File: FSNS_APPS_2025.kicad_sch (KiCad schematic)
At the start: 85 parts, among them J1 Conn_01x04_Pin, J2 Conn_01x03_Pin, J3 Conn_01x03_Pin, J4 Conn_01x02_Socket, K1 PR12-12V-360-1A, Q1 NDT3055L, SW1 SW_Push, U1 STM32F103C8T6, U2 MCP6001-OT, U3 MCP6001-OT, U4 LM1117-Q1, U5 LM1117-Q1, U6 LM1117-Q1, U7 TCAN3404-Q1, U8 LM1117-Q1, Y1 16MHz

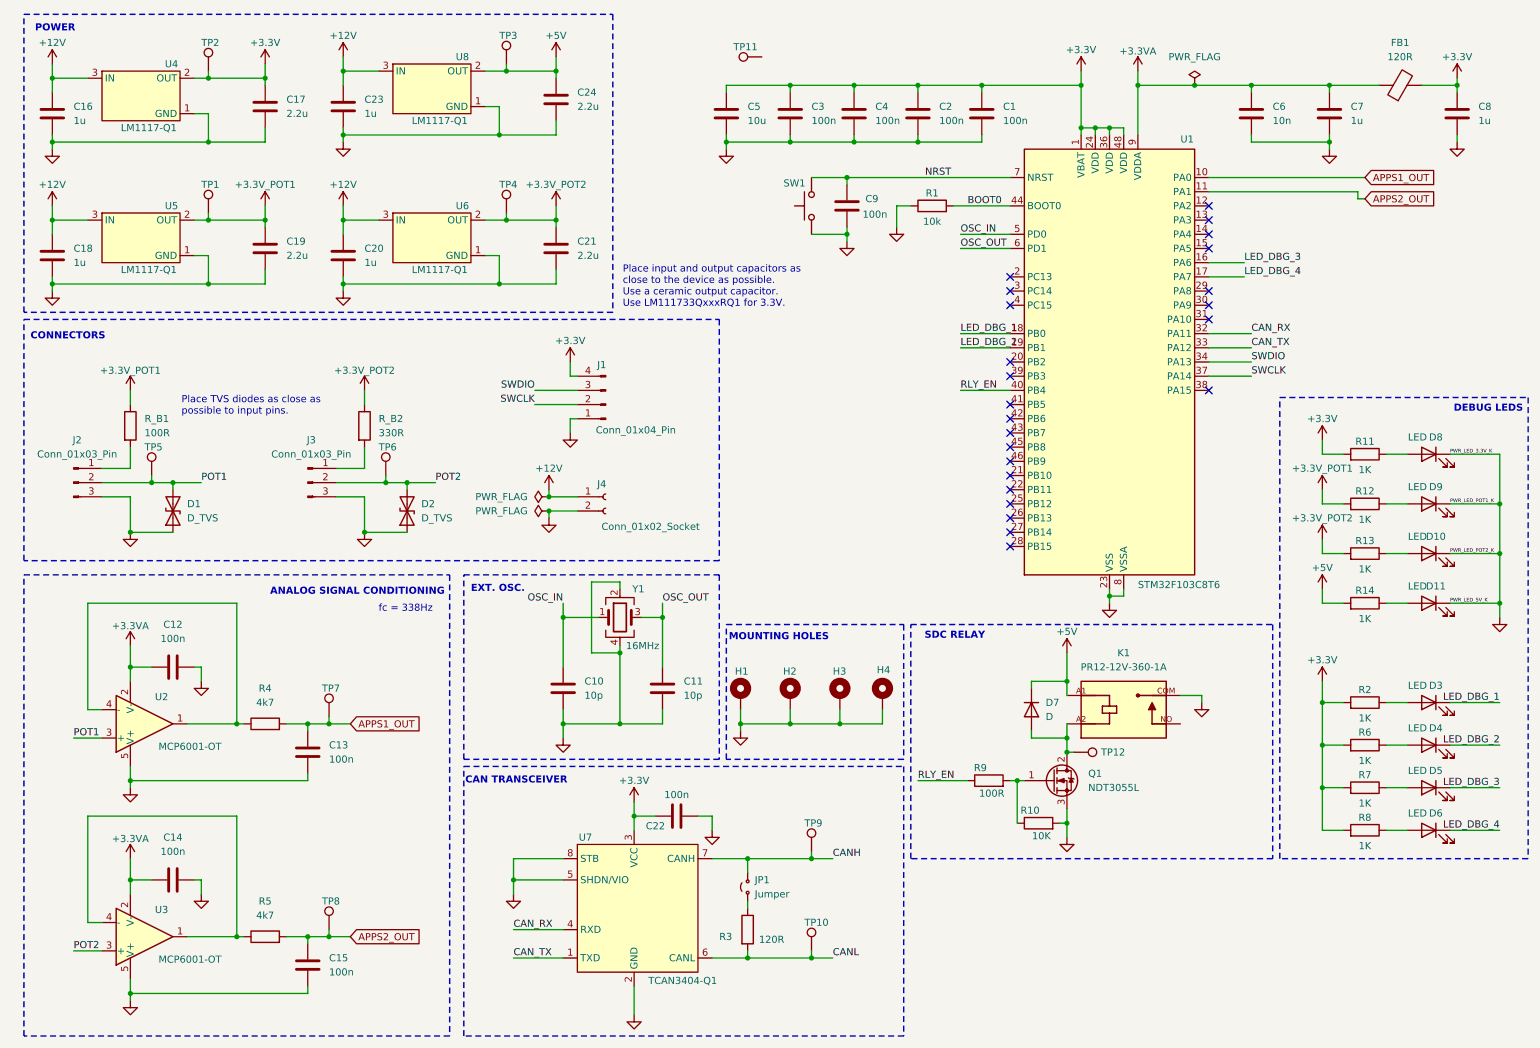
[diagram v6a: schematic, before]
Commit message: Updated schematic and PCB.
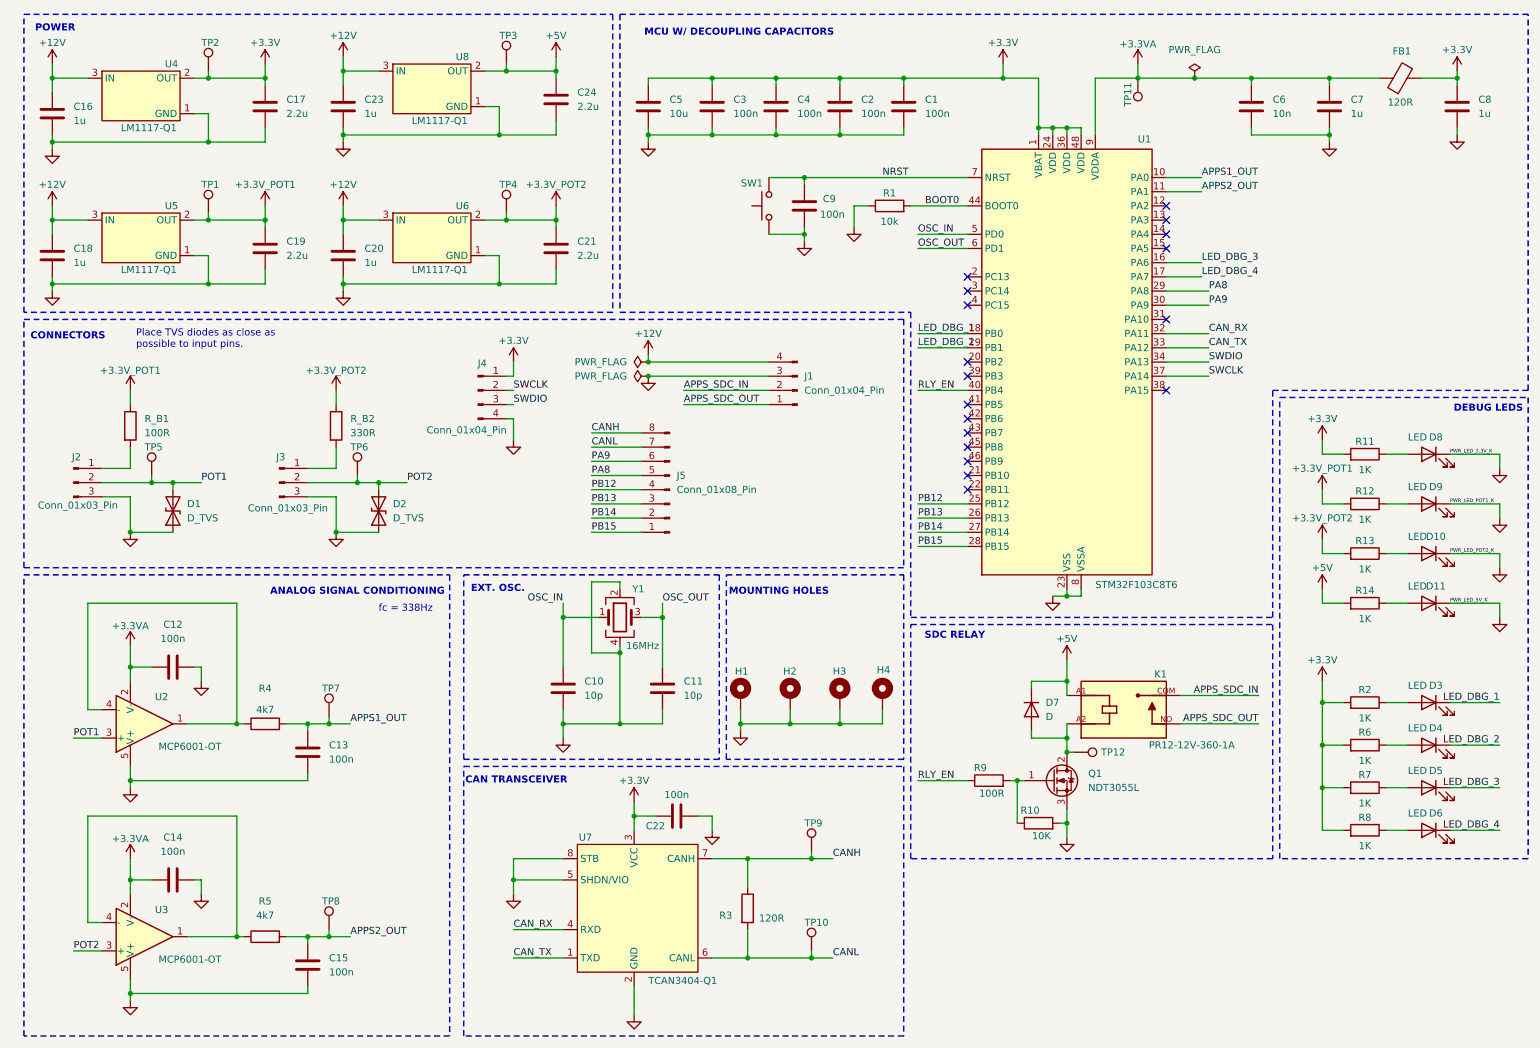
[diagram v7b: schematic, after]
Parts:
- removed J4: Conn_01x02_Socket, symbol Connector:Conn_01x02_Socket
- removed JP1: Jumper, symbol Jumper:Jumper_2_Small_Open
- added J4: Conn_01x04_Pin, Connector_PinHeader_2.54mm:PinHeader_1x04_P2.54mm_Horizontal, symbol Connector:Conn_01x04_Pin
- added J5: Conn_01x08_Pin, Connector_PinSocket_2.54mm:PinSocket_1x08_P2.54mm_Horizontal, symbol Connector:Conn_01x08_Pin
- D1, D2: footprint (none) -> Diode_SMD:D_0603_1608Metric
- D7: footprint (none) -> Diode_SMD:D_1206_3216Metric
- J1: footprint (none) -> MOLEX Micro-Fit 3.0 43045:CONN_SD-43045-005_04_MOL
- J2, J3: footprint (none) -> MOLEX Micro-Fit 3.0 43045:CONN_SD-43650-006_03_MOL
- R3: footprint (none) -> Resistor_SMD:R_0402_1005Metric
- SW1: footprint (none) -> Button_Switch_SMD:SW_SPST_B3S-1000
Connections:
- net +12V: now also J1.4 (Pin_4)
- net +3.3V: now also J4.1 (Pin_1); no longer J1.4 (Pin_4)
- net +3.3VA: now also TP11.1
- net CANH: now also R3.1, J5.8 (Pin_8)
- net CANL: now also J5.7 (Pin_7)
- net GND: now also J1.3 (Pin_3), J4.4 (Pin_4); no longer J1.1 (Pin_1), K1.COM
- net SWCLK: now also J4.2 (Pin_2); no longer J1.2 (Pin_2)
- net SWDIO: now also J4.3 (Pin_3); no longer J1.3 (Pin_3)
- net APPS_SDC_OUT: now reaches K1.NO
- net APPS_SDC_OUT: now also J1.1 (Pin_1)
- net PB12: now reaches U1.25 (PB12)
- net PB12: now also J5.4 (Pin_4)
- net PB13: now reaches U1.26 (PB13)
- net PB13: now also J5.3 (Pin_3)
- net PB14: now reaches U1.27 (PB14)
- net PB14: now also J5.2 (Pin_2)
- net PB15: now reaches U1.28 (PB15)
- net PB15: now also J5.1 (Pin_1)
- net PA8: now reaches U1.29 (PA8)
- net PA8: now also J5.5 (Pin_5)
- net PA9: now reaches U1.30 (PA9)
- net PA9: now also J5.6 (Pin_6)
- new net APPS_SDC_IN: J1.2 (Pin_2), K1.COM
- no-connect marks 24 -> 18
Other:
- note added: "MCU W/ DECOUPLING CAPACITORS"
- note removed: "Place input and output capacitors as close to the device as possible. Use a ceramic output capacitor. Use LM111733QxxxRQ1 for 3.3V."
- moved on the sheet: C1, C2, C3, C4, C5, C6, C7, C8, C9, D2, FB1, J3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

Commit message: Schematic and PCB v0.1
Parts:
- added JP1: SolderJumper_2_Open, symbol Jumper:SolderJumper_2_Open
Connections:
- net CANH: now also JP1.2 (B); no longer R3.1
- net PB12: now also J5.1 (Pin_1); no longer J5.4 (Pin_4)
- net PB13: now also J5.2 (Pin_2); no longer J5.3 (Pin_3)
- net PB14: now also J5.3 (Pin_3); no longer J5.2 (Pin_2)
- net PB15: now also J5.4 (Pin_4); no longer J5.1 (Pin_1)
- new net: JP1.1 (A), R3.1
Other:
- company: (none) -> Black Hornets Novi Sad - Predrag Nuzdic
- title: (none) -> Accelerator Pedal Position Sensor Board
- moved on the sheet: J5, R3
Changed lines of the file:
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@@
 	(generator_version "9.0")
 	(paper "A4")
+	(title_block
+		(title "Accelerator Pedal Position Sensor Board")
+		(date "2026-01-11")
+		(rev "0.1")
+		(company "Black Hornets Novi Sad - Predrag Nuzdic")
+	)
 	(rectangle
 		(start 92.71 113.03)
@@
 	)
 	(junction
+		(at 143.51 163.83)
+		(diameter 0)
+		(color 0 0 0 0)
+	)
+	(junction
 		(at 33.02 187.96)
 		(diameter 0)
@@
 	)
 	(junction
-		(at 143.51 163.83)
-		(diameter 0)
-		(color 0 0 0 0)
-	)
-	(junction
 		(at 46.99 35.56)
 		(diameter 0)
@@
 	(wire
 		(pts
-			(xy 115.57 87.63) (xy 124.46 87.63)
+			(xy 138.43 87.63) (xy 147.32 87.63)
 		)
 		(stroke
@@
 	(wire
 		(pts
+			(xy 143.51 163.83) (xy 143.51 165.1)
+		)
+		(stroke
+			(width 0)
+			(type default)
+		)
+	)
+	(wire
+		(pts
 			(xy 160.02 33.02) (xy 160.02 34.29)
 		)
@@
 	(wire
 		(pts
-			(xy 115.57 90.17) (xy 124.46 90.17)
+			(xy 138.43 90.17) (xy 147.32 90.17)
 		)
 		(stroke
@@
 	(wire
 		(pts
-			(xy 115.57 97.79) (xy 124.46 97.79)
+			(xy 138.43 105.41) (xy 147.32 105.41)
 		)
 		(stroke
@@
 	(wire
 		(pts
-			(xy 143.51 163.83) (xy 154.94 163.83)
+			(xy 137.16 163.83) (xy 143.51 163.83)
 		)
 		(stroke
@@
 	(wire
 		(pts
-			(xy 115.57 100.33) (xy 124.46 100.33)
+			(xy 138.43 102.87) (xy 147.32 102.87)
 		)
 		(stroke
@@
 	(wire
 		(pts
-			(xy 137.16 163.83) (xy 143.51 163.83)
-		)
-		(stroke
-			(width 0)
-			(type default)
-		)
-	)
-	(wire
-		(pts
 			(xy 154.94 180.34) (xy 154.94 181.61)
 		)
@@
 	(wire
 		(pts
-			(xy 115.57 95.25) (xy 124.46 95.25)
+			(xy 138.43 95.25) (xy 147.32 95.25)
 		)
 		(stroke
@@
 	(wire
 		(pts
-			(xy 143.51 163.83) (xy 143.51 168.91)
-		)
-		(stroke
-			(width 0)
-			(type default)
-		)
-	)
-	(wire
-		(pts
 			(xy 96.52 55.88) (xy 99.06 55.88)
 		)
@@
 	(wire
 		(pts
-			(xy 115.57 102.87) (xy 124.46 102.87)
+			(xy 138.43 100.33) (xy 147.32 100.33)
 		)
 		(stroke
@@
 	(wire
 		(pts
-			(xy 115.57 92.71) (xy 124.46 92.71)
+			(xy 138.43 92.71) (xy 147.32 92.71)
 		)
 		(stroke
@@
 	(wire
 		(pts
-			(xy 143.51 176.53) (xy 143.51 181.61)
+			(xy 143.51 180.34) (xy 143.51 181.61)
 		)
 		(stroke
@@
 	(wire
 		(pts
-			(xy 115.57 105.41) (xy 124.46 105.41)
+			(xy 138.43 97.79) (xy 147.32 97.79)
 		)
 		(stroke
@@
 	(wire
 		(pts
+			(xy 143.51 163.83) (xy 154.94 163.83)
+		)
+		(stroke
+			(width 0)
+			(type default)
+		)
+	)
+	(wire
+		(pts
 			(xy 57.15 33.02) (xy 57.15 35.56)
 		)
@@
 	)
 	(label "PB14"
-		(at 115.57 102.87 0)
+		(at 138.43 100.33 0)
 		(effects
 			(font
@@
 	)
 	(label "CANH"
-		(at 115.57 87.63 0)
+		(at 138.43 87.63 0)
 		(effects
 			(font
@@
 	)
 	(label "PA8"
-		(at 115.57 95.25 0)
+		(at 138.43 95.25 0)
 		(effects
 			(font
@@
 	)
 	(label "PB13"
-		(at 115.57 100.33 0)
+		(at 138.43 102.87 0)
 		(effects
 			(font
@@
 	)
 	(label "CANL"
-		(at 115.57 90.17 0)
+		(at 138.43 90.17 0)
 		(effects
 			(font
@@
 	)
 	(label "PB12"
-		(at 115.57 97.79 0)
+		(at 138.43 105.41 0)
 		(effects
 			(font
@@
 	)
 	(label "PB15"
-		(at 115.57 105.41 0)
+		(at 138.43 97.79 0)
 		(effects
 			(font
@@
 	)
 	(label "PA9"
-		(at 115.57 92.71 0)
+		(at 138.43 92.71 0)
 		(effects
 			(font
@@
 	(symbol
 		(lib_id "Connector:Conn_01x08_Pin")
-		(at 129.54 97.79 180)
+		(at 152.4 97.79 180)
 		(unit 1)
 		(exclude_from_sim no)
@@
 		(on_board yes)
 		(dnp no)
-		(fields_autoplaced yes)
 		(property "Reference" "J5"
-			(at 130.81 95.2499 0)
+			(at 150.368 85.852 0)
 			(effects
 				(font
@@
 		)
 		(property "Value" "Conn_01x08_Pin"
-			(at 130.81 97.7899 0)
+			(at 142.494 107.188 0)
 			(effects
 				(font
@@
 		)
 		(property "Footprint" "Connector_PinSocket_2.54mm:PinSocket_1x08_P2.54mm_Horizontal"
-			(at 129.54 97.79 0)
+			(at 152.4 97.79 0)
 			(effects
 				(font
@@
 		)
 		(property "Datasheet" "~"
-			(at 129.54 97.79 0)
+			(at 152.4 97.79 0)
 			(effects
 				(font
@@
 		)
 		(property "Description" "Generic connector, single row, 01x08, script generated"
-			(at 129.54 97.79 0)
+			(at 152.4 97.79 0)
 			(effects
 				(font
@@
 		(on_board yes)
 		(dnp no)
-		(fields_autoplaced yes)
 		(property "Reference" "J1"
-			(at 153.67 77.4699 0)
+			(at 150.368 73.152 0)
 			(effects
 				(font
@@
 		)
 		(property "Value" "Conn_01x04_Pin"
-			(at 153.67 80.0099 0)
+			(at 150.622 83.82 0)
 			(effects
 				(font
@@
 	)
 	(symbol
+		(lib_id "Jumper:SolderJumper_2_Open")
+		(at 143.51 168.91 90)
+		(unit 1)
+		(exclude_from_sim no)
+		(in_bom no)
+		(on_board yes)
+		(dnp no)
+		(fields_autoplaced yes)
+		(property "Reference" "JP1"
+			(at 146.05 167.6399 90)
+			(effects
+				(font
+					(size 1.27 1.27)
+				)
+				(justify right)
+			)
+		)
+		(property "Value" "SolderJumper_2_Open"
+			(at 146.05 170.1799 90)
+			(effects
+				(font
+					(size 1.27 1.27)
+				)
+				(justify right)
+				(hide yes)
+			)
+		)
+		(property "Footprint" ""
+			(at 143.51 168.91 0)
+			(effects
+				(font
+					(size 1.27 1.27)
+				)
+				(hide yes)
+			)
+		)
+		(property "Datasheet" "~"
+			(at 143.51 168.91 0)
+			(effects
+				(font
+					(size 1.27 1.27)
+				)
+				(hide yes)
+			)
+		)
+		(property "Description" "Solder Jumper, 2-pole, open"
+			(at 143.51 168.91 0)
+			(effects
+				(font
+					(size 1.27 1.27)
+				)
+				(hide yes)
+			)
+		)
+		(pin "2"
+		)
+		(pin "1"
+		)
+		(instances
+			(project ""
+				(path "/84b2f9c6-f788-4685-8b6c-d48d40cc3830"
+					(reference "JP1")
+					(unit 1)
+				)
+			)
+		)
+	)
+	(symbol
 		(lib_id "Device:C")
 		(at 233.68 29.21 0)
@@
 	(symbol
 		(lib_id "Device:R")
-		(at 143.51 172.72 0)
+		(at 143.51 176.53 0)
 		(unit 1)
 		(exclude_from_sim no)
@@
 		(dnp no)
 		(property "Reference" "R3"
-			(at 138.43 173.99 0)
+			(at 138.43 177.8 0)
 			(effects
 				(font
@@
 		)
 		(property "Value" "120R"
-			(at 145.542 174.498 0)
+			(at 145.542 178.308 0)
 			(effects
 				(font
@@
 		)
 		(property "Footprint" "Resistor_SMD:R_0402_1005Metric"
-			(at 141.732 172.72 90)
+			(at 141.732 176.53 90)
 			(effects
 				(font
@@
 		)
 		(property "Datasheet" "~"
-			(at 143.51 172.72 0)
+			(at 143.51 176.53 0)
 			(effects
 				(font
@@
 		)
 		(property "Description" "Resistor"
-			(at 143.51 172.72 0)
+			(at 143.51 176.53 0)
 			(effects
 				(font
